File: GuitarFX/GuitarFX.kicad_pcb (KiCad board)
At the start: 4 copper layers, 70 x 85 mm, 122 parts, among them IC401 PCM3060PWR, J202 Screw_Terminal_01x02, J301 USB_C_Receptacle_USB2.0, J302 Conn_ARM_SWD_TagConnect_TC2030, J303 Screw_Terminal_01x06, J401 Screw_Terminal_01x02, J402 Screw_Terminal_01x02, SW301 SW_SPDT, U201 NCP718xSN500, U202 NCP1117-3.3_SOT223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

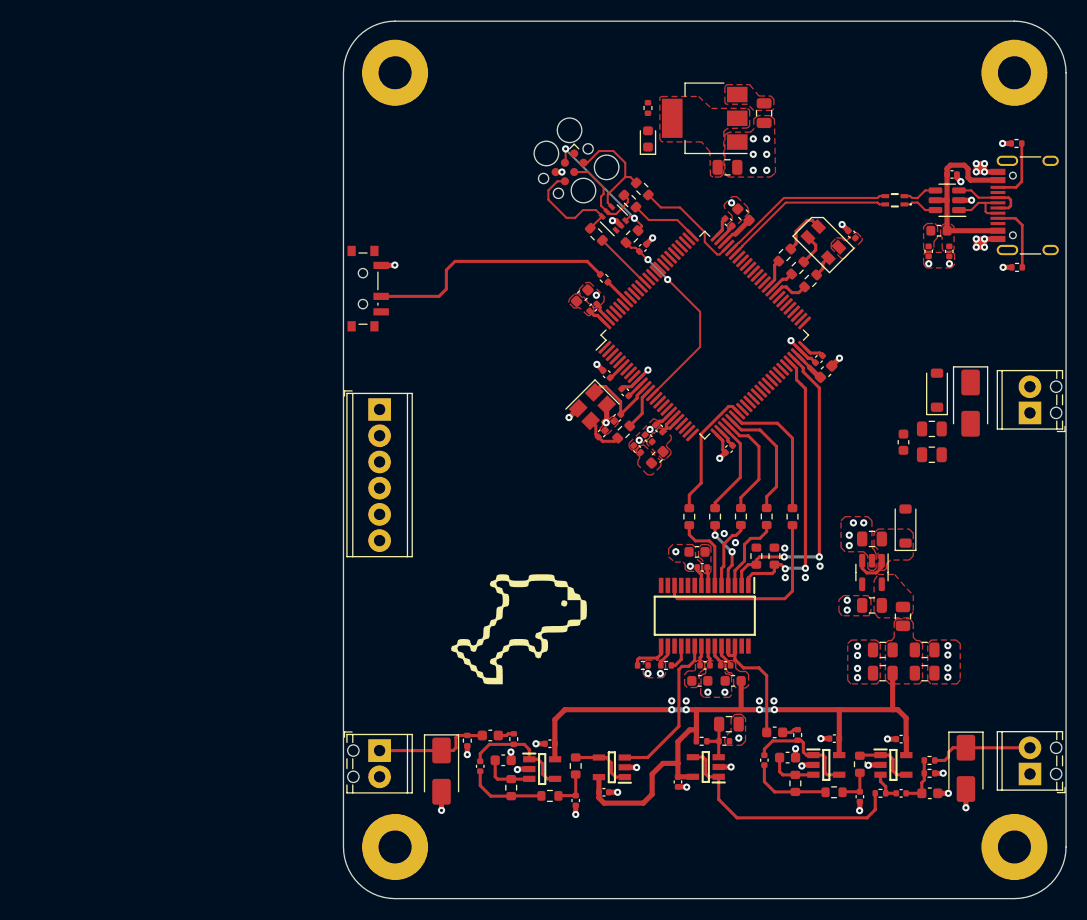
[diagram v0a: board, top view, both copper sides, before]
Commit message: Finished 3V power routing
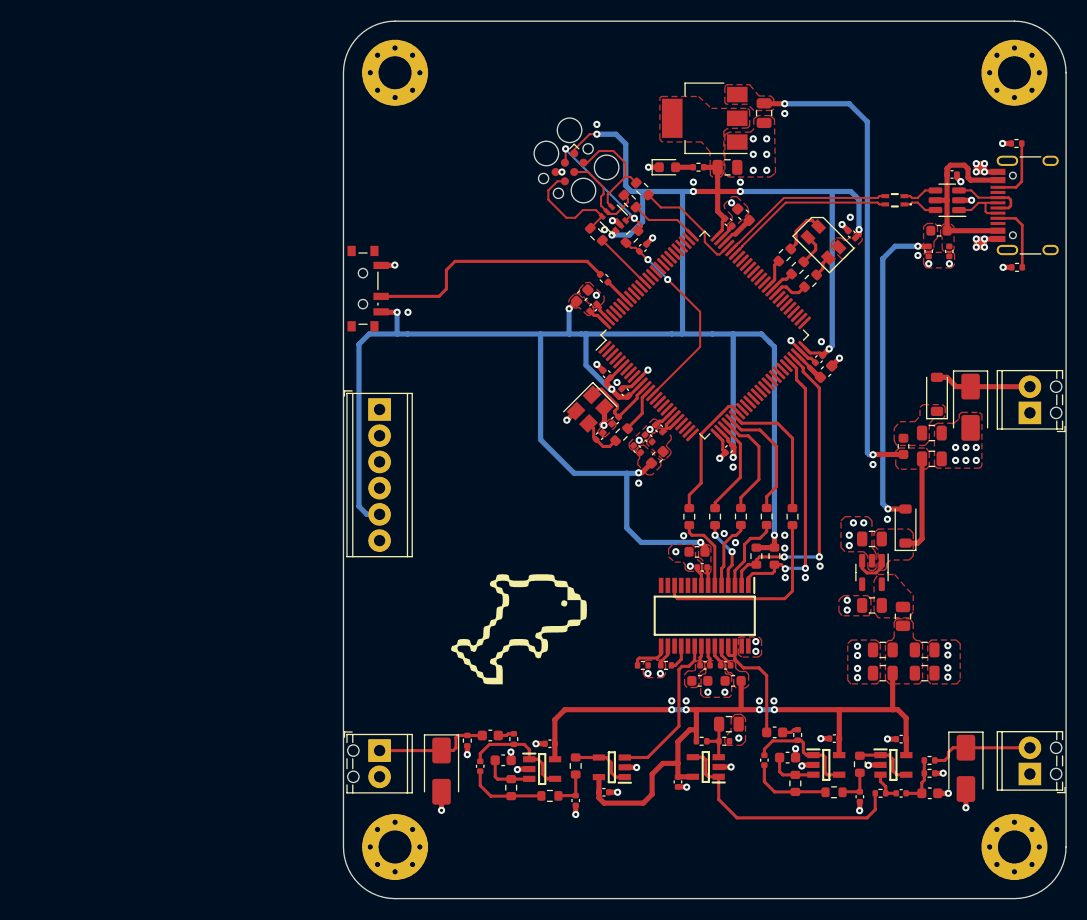
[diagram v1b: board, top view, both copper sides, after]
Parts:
- H101, H102, H103, H104: footprint MountingHole:MountingHole_3.2mm_M3_Pad -> MountingHole:MountingHole_3.2mm_M3_Pad_Via
- moved R202 7.54 mm to (144.4, 72.7), turned to 180 degrees
- moved D204 3.33 mm to (141.4, 72.7), turned to 0 degrees
- moved C205 0.40 mm to (167.0, 98.4)
- moved C206 0.40 mm to (167.0, 100.9)
- moved D202 0.40 mm to (167.5, 94.7)
- moved D203 0.40 mm to (170.8, 95.9)
- moved FB201 0.40 mm to (164.2, 99.7)
- moved C314 0.33 mm to (136.3, 97.2)
- moved C315 0.33 mm to (134.8, 98.7)
- moved R302 0.33 mm to (136.9, 98.6)
- moved Y301 0.33 mm to (133.9, 96.1)
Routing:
- net +3.3V: track 13.0 -> 243.4 mm, vias 0 -> 13
- net /Power/VCC_FILT: track 3.67 -> 59.6 mm, vias 0 -> 2
- net VUSB_FILT: track 0.00 -> 31.1 mm, vias 0 -> 2
- net VCC: track 0.00 -> 9.38 mm
- net /Power/R_LED: track 0.00 -> 1.70 mm
- net GND: track 70.0 -> 71.0 mm, vias 86 -> 111
- added copper zone on F.Cu, net /Power/VCC_RP

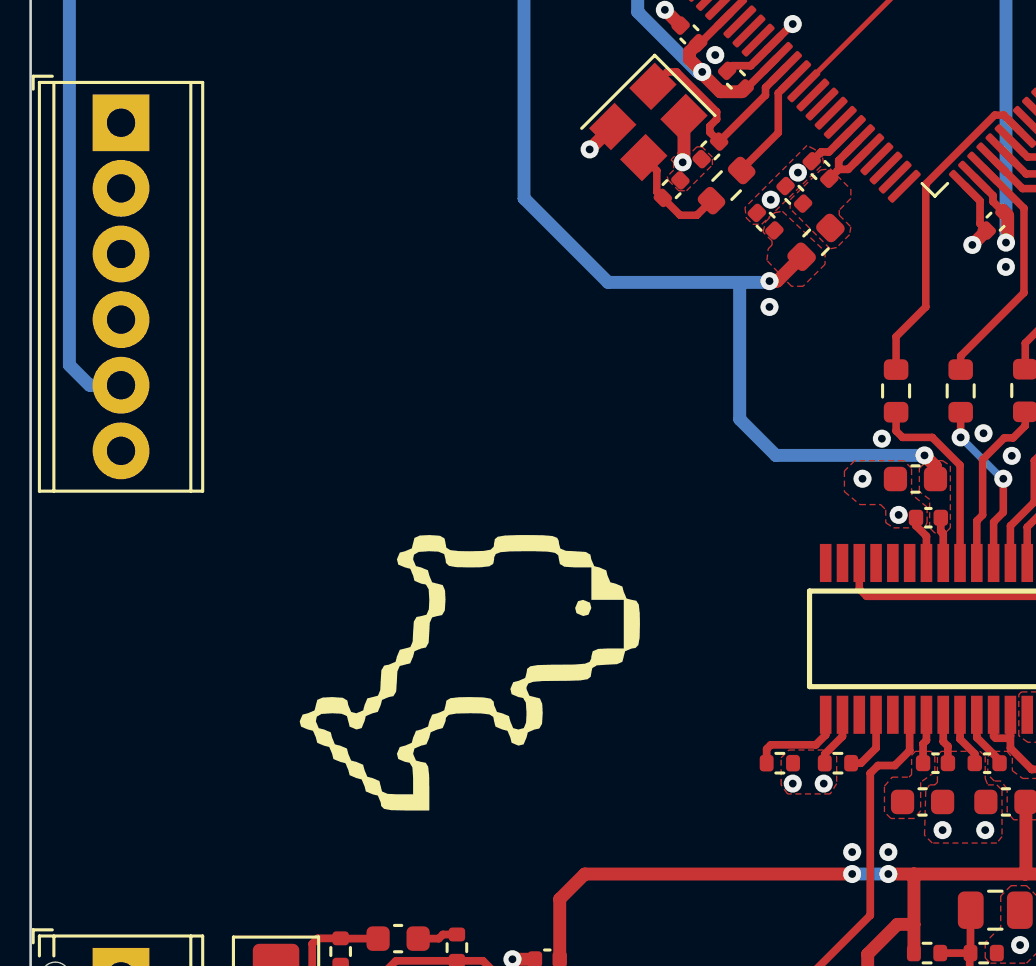
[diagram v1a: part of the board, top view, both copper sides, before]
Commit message: Added pi filter for Codec NRST signal
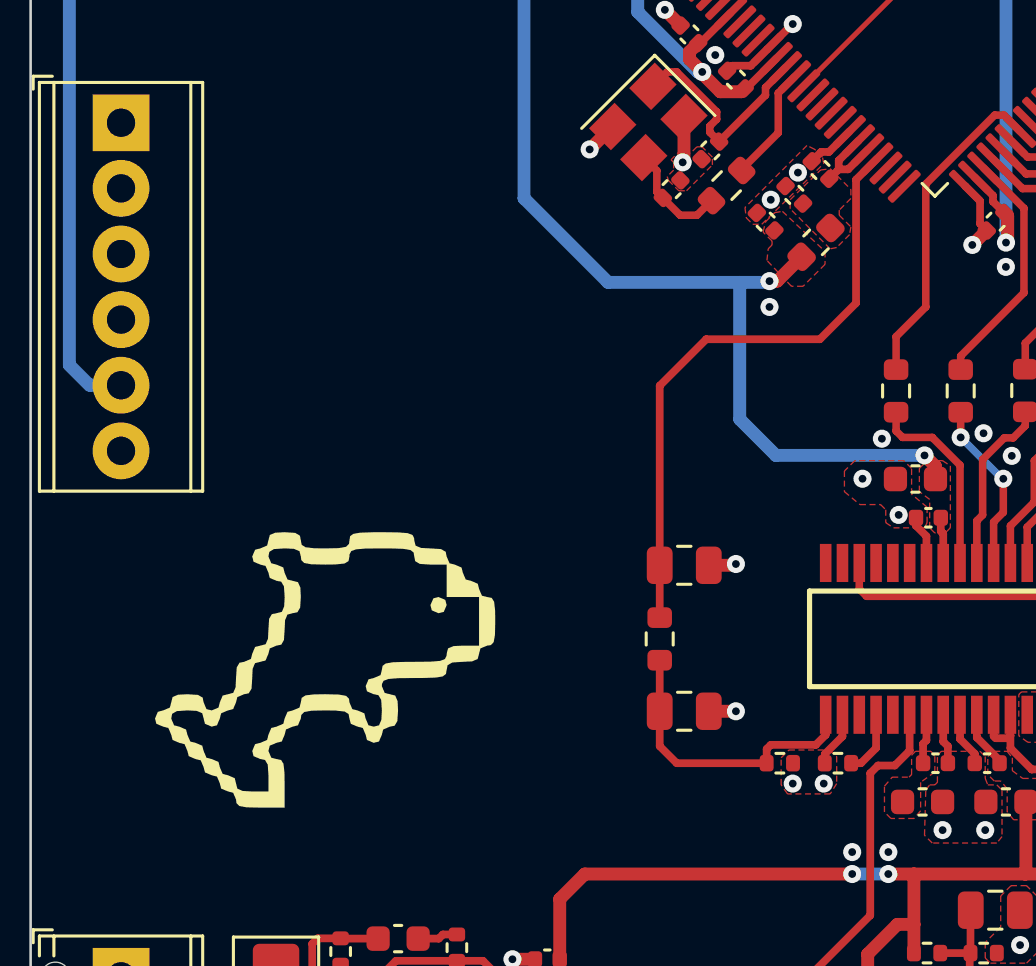
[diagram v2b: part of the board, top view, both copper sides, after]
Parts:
- added C411: 2.2uF, Capacitor_SMD:C_0805_2012Metric, F.Cu at (135.3, 113.2)
- added C412: 2.2uF, Capacitor_SMD:C_0805_2012Metric, F.Cu at (135.3, 118.9)
- added R411: 5.1k, Resistor_SMD:R_0603_1608Metric, F.Cu at (134.3, 116.1)
- moved G*** 5.60 mm to (121.1, 120.1)
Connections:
- IC401 pad 15: CODEC_NRST -> /Codec/NRST_FILT
- R429 pad 1: CODEC_NRST -> /Codec/NRST_FILT
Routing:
- net CODEC_NRST: track 3.84 -> 23.8 mm
- net /Codec/NRST_FILT: track 0.00 -> 11.6 mm
- net GND: track 71.0 -> 73.2 mm, vias 111 -> 113

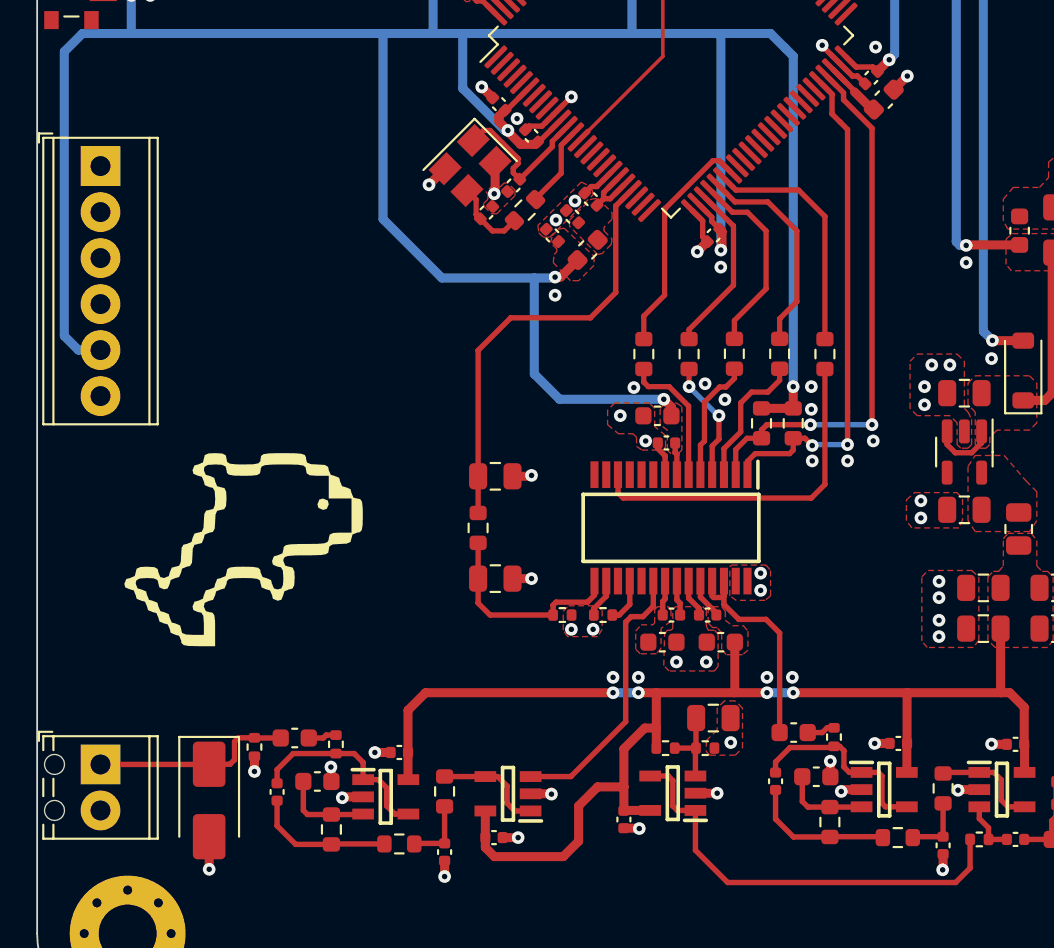
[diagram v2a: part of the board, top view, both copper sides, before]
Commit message: Completed ADC terminal block connections. Finished routing
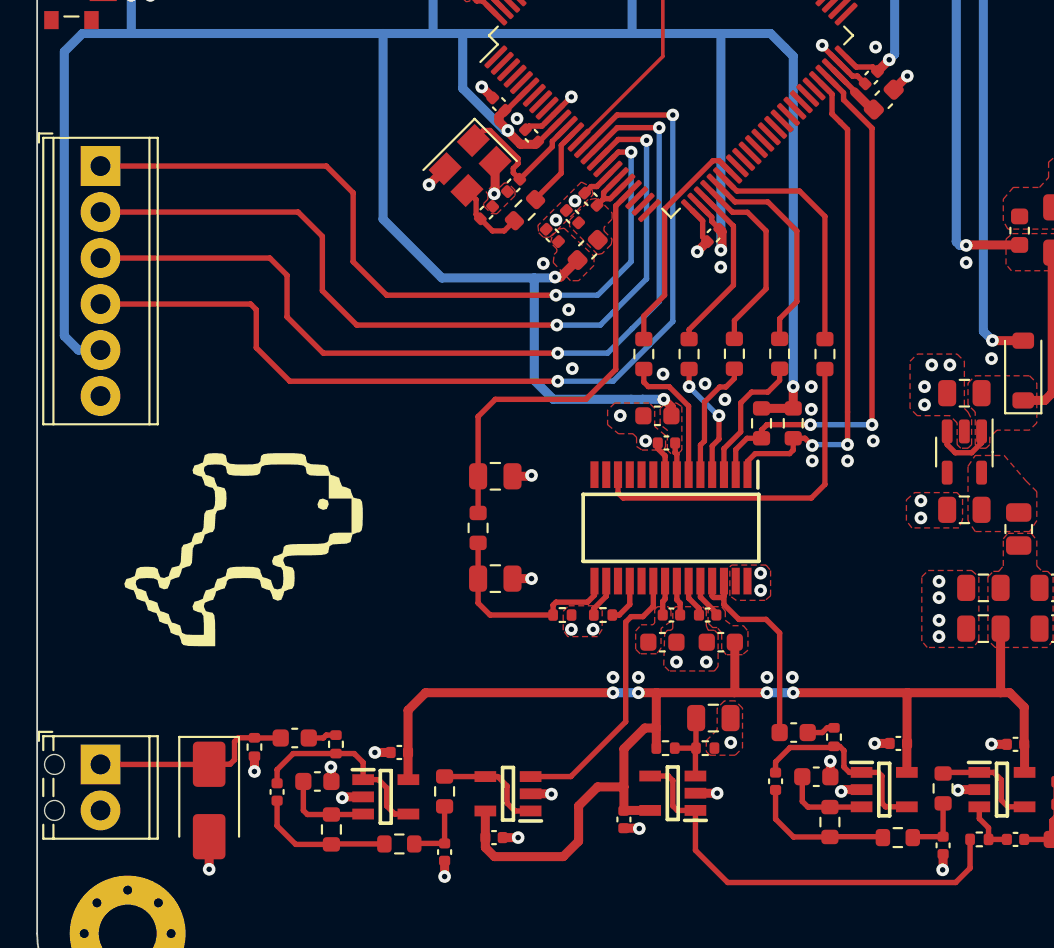
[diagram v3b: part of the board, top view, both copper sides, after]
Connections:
- J303 pad 1: /MCU/ADC3_INP10 -> /MCU/ADC3_INP1
- J303 pad 2: /MCU/ADC3_INP11 -> /MCU/ADC3_INP0
- J303 pad 3: /MCU/ADC3_INP0 -> /MCU/ADC3_INP11
- J303 pad 4: /MCU/ADC3_INP1 -> /MCU/ADC3_INP10
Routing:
- net /MCU/ADC3_INP10: track 0.00 -> 52.9 mm, vias 0 -> 2
- net /MCU/ADC3_INP11: track 0.00 -> 49.4 mm, vias 0 -> 2
- net /MCU/ADC3_INP0: track 0.00 -> 46.3 mm, vias 0 -> 2
- net /MCU/ADC3_INP1: track 0.00 -> 43.1 mm, vias 0 -> 2
- net GND: track 73.2 -> 73.1 mm, vias 113 -> 115

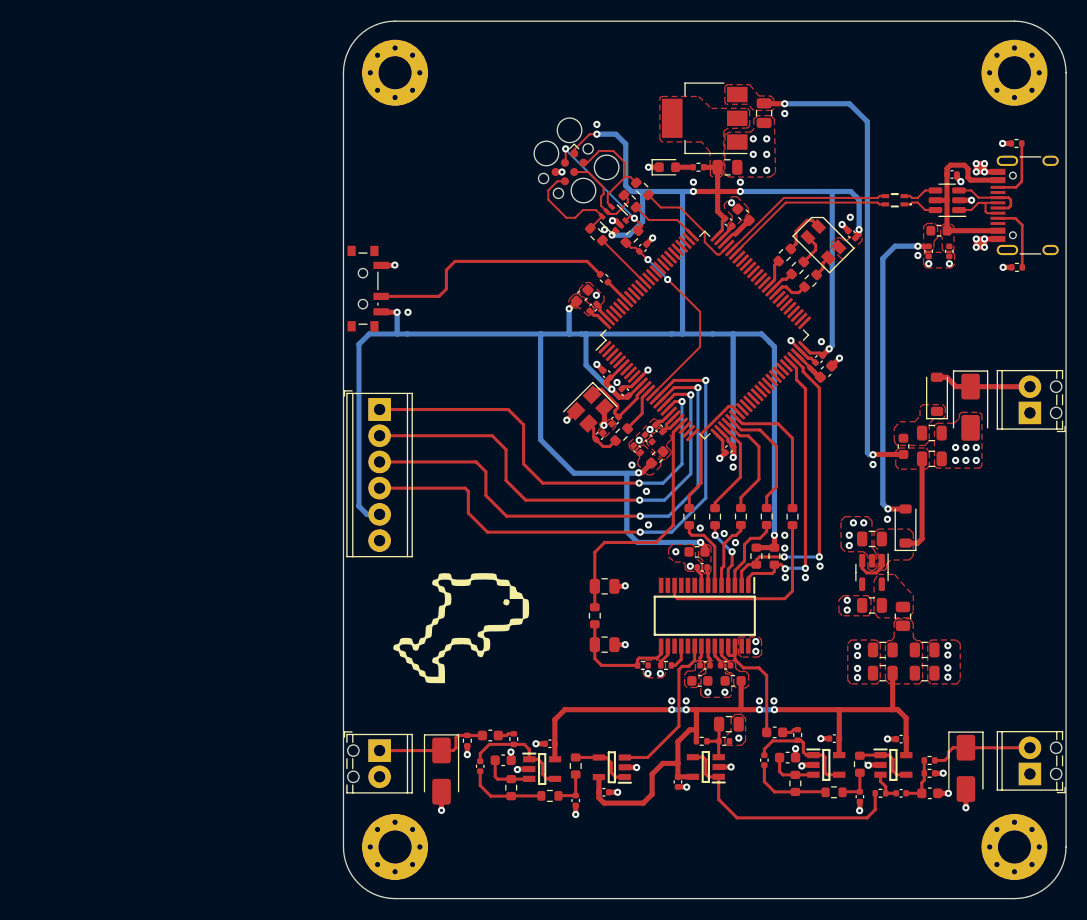
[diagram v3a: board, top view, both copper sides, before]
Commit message: Fixed errors in DRC
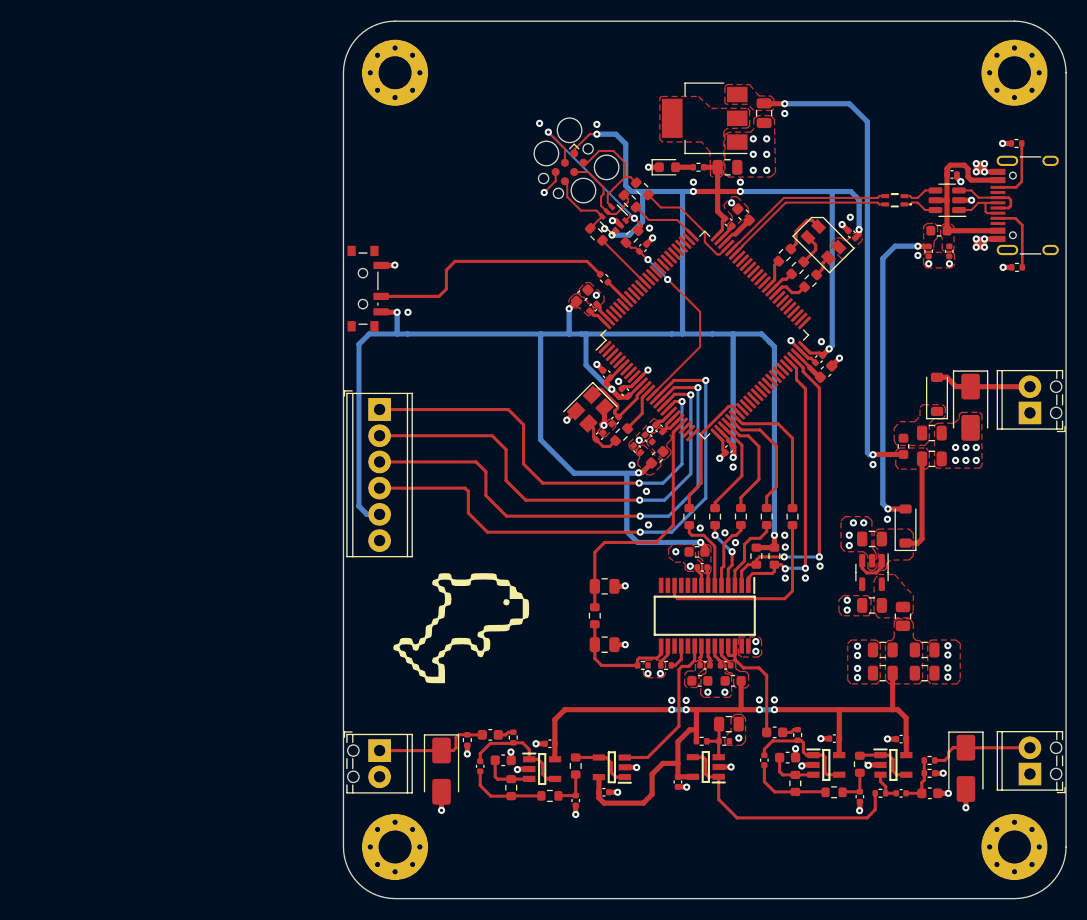
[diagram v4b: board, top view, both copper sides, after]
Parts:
- moved R425 0.16 mm to (126.5, 127.9)
- moved C422 0.06 mm to (124.2, 127.6)
- moved R427 0.06 mm to (122.0, 128.1)
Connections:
- J301 pad S1: unconnected-(J301-SHIELD-PadS1) -> (no net)
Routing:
- net /MCU/NRST: track 13.6 -> 18.2 mm
- net /MCU/SWO: track 11.0 -> 7.41 mm
- net GND: track 73.1 -> 75.0 mm, vias 115 -> 117
- net /MCU/MCU_VCAP1: track 4.14 -> 3.17 mm

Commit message: Added stitching vias
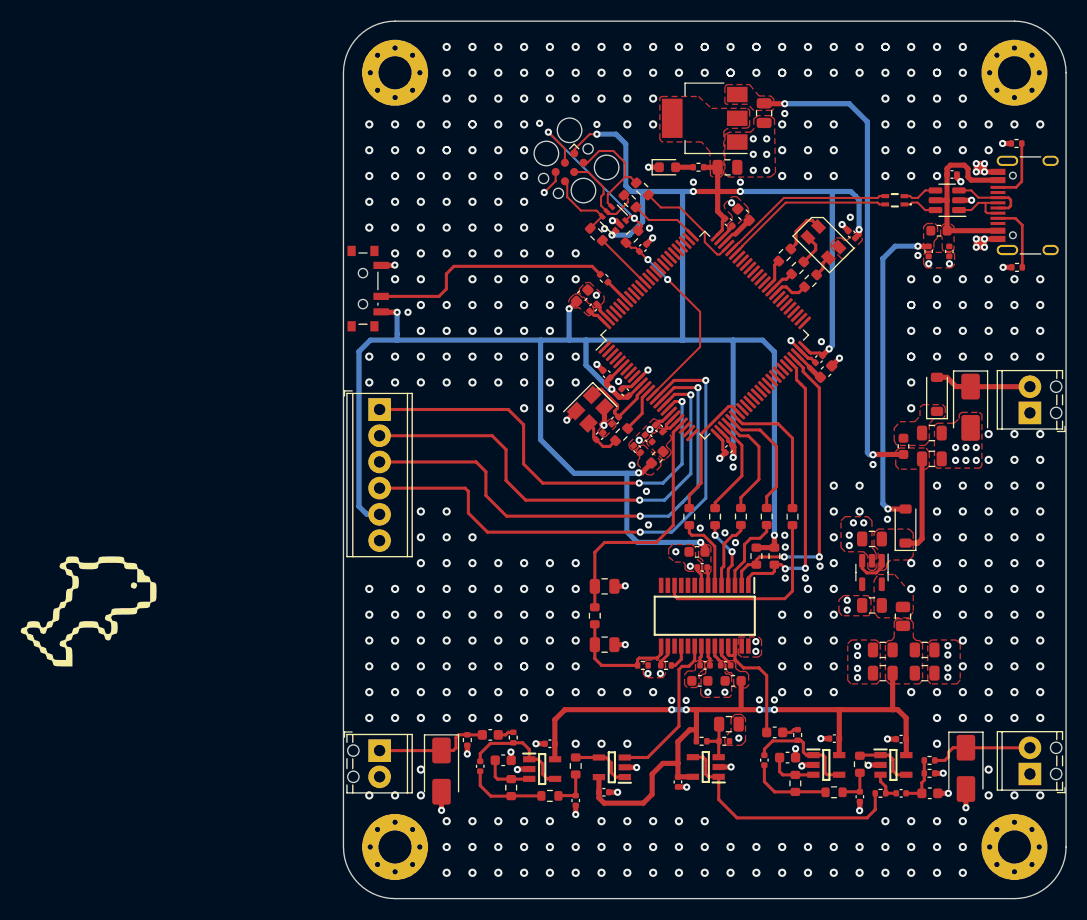
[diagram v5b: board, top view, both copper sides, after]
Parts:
- moved G*** 36.1 mm to (85.0, 118.5)
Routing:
- net +3.3V: track 243.6 -> 242.3 mm
- net Net-(SW301-B): track 24.3 -> 23.6 mm
- net GND: vias 117 -> 533
